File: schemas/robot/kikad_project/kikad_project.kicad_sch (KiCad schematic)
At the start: 50 parts, among them IC1 HCPL-2531, IC2 HCPL-2531, IC3 HCPL-2531, J1 236-102, J10 236-104, J11 236-104, J12 236-744, J13 236-102, J14 236-102, J15 236-102, J16 236-102, J17 236-744, J18 236-102, J2 236-104, J3 236-102, J4 236-102, J5 236-744, J6 236-102, J7 236-102, J8 236-744, J9 236-102, Q2 IRF5305PbF, U1 NRF24L01_Breakout, U12 CD40109BE, U2 STM32F103C8T6, U3 L7805, U4 L7805, X1 3522-2

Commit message: small edits to robot PCB schema and pcb layout
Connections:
- net DISK_DIR: now also IC1.4 (VF2+), U2.14 (PA4); no longer IC1.3 (VIN-), U2.16 (PA6)
- net DISK_PWM: now also IC1.1 (VF1+); no longer IC1.2 (VIN+)
- net GND: now also IC1.2 (VF1-), IC1.3 (VF2-), IC2.2 (VF1-), IC2.3 (VF2-), IC3.2 (VF1-), IC3.3 (VF2-); no longer IC1.4 (GND1), IC2.4 (GND1), IC3.4 (GND1)
- net VCC: no longer IC1.1 (VDD1), IC2.1 (VDD1), IC3.1 (VDD1)
- net WHEEL_LEFT_DIR: now also IC2.4 (VF2+); no longer IC2.3 (VIN-)
- net WHEEL_LEFT_PWM: now also IC2.1 (VF1+); no longer IC2.2 (VIN+)
- net WHEEL_RIGHT_DIR: now also IC3.4 (VF2+), U2.16 (PA6); no longer IC3.3 (VIN-), U2.14 (PA4)
- net WHEEL_RIGHT_PWM: now also IC3.1 (VF1+); no longer IC3.2 (VIN+)

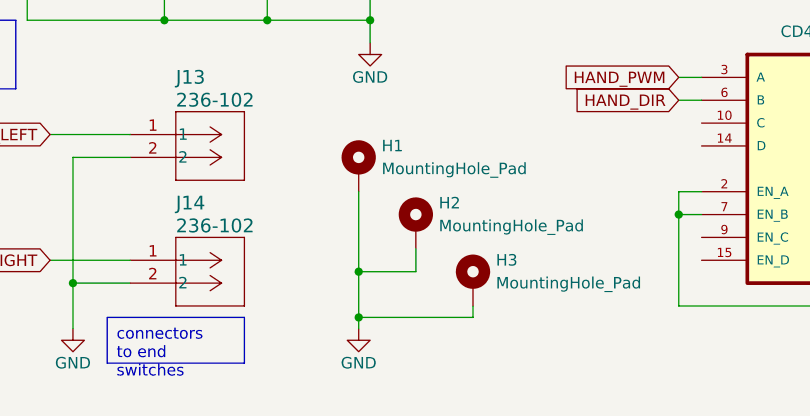
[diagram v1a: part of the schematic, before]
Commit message: small changes to the PCB layout
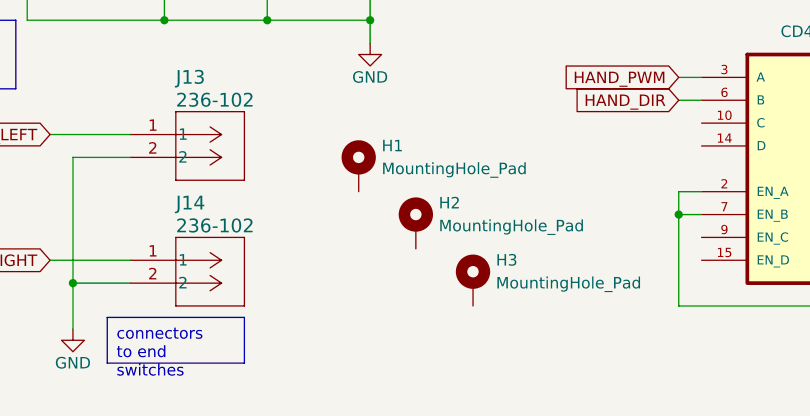
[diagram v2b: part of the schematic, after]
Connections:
- net GND: no longer H1.1, H2.1, H3.1
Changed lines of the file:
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@@
   (junction (at 135.89 161.29) (diameter 0) (color 0 0 0 0)
   )
-  (junction (at 68.58 182.88) (diameter 0) (color 0 0 0 0)
-  )
   (junction (at 238.76 143.51) (diameter 0) (color 0 0 0 0)
   )
@@
   (junction (at 140.97 185.42) (diameter 0) (color 0 0 0 0)
   )
-  (junction (at 68.58 187.96) (diameter 0) (color 0 0 0 0)
-  )
   (junction (at 58.42 142.24) (diameter 0) (color 0 0 0 0)
   )
@@
     (stroke (width 0) (type default))
   )
-  (wire (pts (xy 68.58 182.88) (xy 74.93 182.88))
-    (stroke (width 0) (type default))
-  )
   (wire (pts (xy 109.22 63.5) (xy 111.76 63.5))
     (stroke (width 0) (type default))
@@
     (stroke (width 0) (type default))
   )
-  (wire (pts (xy 68.58 187.96) (xy 68.58 189.23))
-    (stroke (width 0) (type default))
-  )
   (wire (pts (xy 46.99 83.82) (xy 46.99 87.63))
     (stroke (width 0) (type default))
@@
     (stroke (width 0) (type default))
   )
-  (wire (pts (xy 68.58 173.99) (xy 68.58 182.88))
-    (stroke (width 0) (type default))
-  )
   (wire (pts (xy 142.24 63.5) (xy 144.78 63.5))
     (stroke (width 0) (type default))
@@
     (stroke (width 0) (type default))
   )
-  (wire (pts (xy 74.93 180.34) (xy 74.93 182.88))
-    (stroke (width 0) (type default))
-  )
   (wire (pts (xy 140.97 168.91) (xy 140.97 173.99))
     (stroke (width 0) (type default))
@@
     (stroke (width 0) (type default))
   )
-  (wire (pts (xy 68.58 182.88) (xy 68.58 187.96))
-    (stroke (width 0) (type default))
-  )
   (wire (pts (xy 140.97 163.83) (xy 140.97 161.29))
     (stroke (width 0) (type default))
@@
     (stroke (width 0) (type default))
   )
-  (wire (pts (xy 68.58 187.96) (xy 81.28 187.96))
-    (stroke (width 0) (type default))
-  )
   (wire (pts (xy 69.85 86.36) (xy 69.85 87.63))
     (stroke (width 0) (type default))
@@
   )
   (wire (pts (xy 238.76 38.1) (xy 243.84 38.1))
-    (stroke (width 0) (type default))
-  )
-  (wire (pts (xy 81.28 186.69) (xy 81.28 187.96))
     (stroke (width 0) (type default))
   )
@@
         )
       )
-    )
-  )
-  (symbol (lib_id "power:GND") (at 68.58 189.23 0) (unit 1)
-    (in_bom yes) (on_board yes) (dnp no)
-    (property "Reference" "#PWR020" (at 68.58 195.58 0)
-      (effects (font (size 1.27 1.27)) hide)
-    )
-    (property "Value" "GND" (at 68.58 193.04 0)
-      (effects (font (size 1.27 1.27)))
-    )
-    (property "Footprint" "" (at 68.58 189.23 0)
-      (effects (font (size 1.27 1.27)) hide)
-    )
-    (property "Datasheet" "" (at 68.58 189.23 0)
-      (effects (font (size 1.27 1.27)) hide)
-    )
-    (pin "1")
-    (instances
-      (project "kikad_project"
-        (path "/d2a66178-d1ee-482f-bb26-256f544868a0"
-          (reference "#PWR020") (unit 1)
-        )
-      )

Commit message: regular upload
1. mid production documentation
2. minor edits on the electrical schemas
3. small changes to the 3d model of the robot
4. first try to wrtie the necessary code
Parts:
- C10: value 100uF -> 10nF
- C11, C12: value 100uF -> 10F
- J12, J17, J5, J8: value 236-744 -> 236-401
- Q2: value IRF5305PbF -> IXTP120P065T
- R2, R3, R4: value 6.8МR -> 68R
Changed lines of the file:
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@@
+    (effects (font (size 1.27 1.27)) (justify left top))
+  )
+  (text_box "diod da pazi da ne se razredqt kondenzatorite"
+    (at 19.05 78.74 0) (size 3.81 3.81)
+    (stroke (width 0) (type default))
+    (fill (type none))
     (effects (font (size 1.27 1.27)) (justify left top))
   )
@@
   (symbol (lib_id "Device:C") (at 123.19 138.43 0) (mirror y) (unit 1)
     (in_bom yes) (on_board yes) (dnp no)
-    (property "Reference" "C12" (at 127 135.89 0)
-      (effects (font (size 1.27 1.27)) (justify left))
-    )
-    (property "Value" "100uF" (at 130.81 140.97 0)
+    (property "Reference" "C12" (at 128.27 135.89 0)
+      (effects (font (size 1.27 1.27)) (justify left))
+    )
+    (property "Value" "10F" (at 128.27 140.97 0)
       (effects (font (size 1.27 1.27)) (justify left))
     )
@@
       (effects (font (size 1.27 1.27)) (justify left))
     )
-    (property "Value" "6.8МR" (at 134.62 134.62 90)
+    (property "Value" "68R" (at 134.62 134.62 90)
       (effects (font (size 1.27 1.27)) (justify left))
     )
@@
       (effects (font (size 1.27 1.27)))
     )
-    (property "Value" "IRF5305PbF" (at 58.42 128.27 90)
+    (property "Value" "IXTP120P065T" (at 58.42 128.27 90)
       (effects (font (size 1.27 1.27)))
     )
@@
   (symbol (lib_id "Device:C") (at 123.19 102.87 0) (mirror y) (unit 1)
     (in_bom yes) (on_board yes) (dnp no)
-    (property "Reference" "C10" (at 127 100.33 0)
-      (effects (font (size 1.27 1.27)) (justify left))
-    )
-    (property "Value" "100uF" (at 130.81 105.41 0)
+    (property "Reference" "C10" (at 128.27 100.33 0)
+      (effects (font (size 1.27 1.27)) (justify left))
+    )
+    (property "Value" "10nF" (at 129.54 105.41 0)
       (effects (font (size 1.27 1.27)) (justify left))
     )
@@
       (effects (font (size 1.27 1.27)) (justify left))
     )
-    (property "Value" "6.8МR" (at 134.62 116.84 90)
+    (property "Value" "68R" (at 134.62 116.84 90)
       (effects (font (size 1.27 1.27)) (justify left))
     )
@@
       (effects (font (size 1.524 1.524)) (justify left))
     )
-    (property "Value" "236-744" (at 248.92 85.09 0)
+    (property "Value" "236-401" (at 248.92 85.09 0)
       (effects (font (size 1.524 1.524)) (justify left))
     )
@@
   (symbol (lib_id "Device:C") (at 123.19 120.65 0) (mirror y) (unit 1)
     (in_bom yes) (on_board yes) (dnp no)
-    (property "Reference" "C11" (at 127 118.11 0)
-      (effects (font (size 1.27 1.27)) (justify left))
-    )
-    (property "Value" "100uF" (at 130.81 123.19 0)
+    (property "Reference" "C11" (at 128.27 118.11 0)
+      (effects (font (size 1.27 1.27)) (justify left))
+    )
+    (property "Value" "10F" (at 128.27 123.19 0)
       (effects (font (size 1.27 1.27)) (justify left))
     )
@@
       (effects (font (size 1.524 1.524)) (justify left))
     )
-    (property "Value" "236-744" (at 152.4 130.81 0)
+    (property "Value" "236-401" (at 152.4 130.81 0)
       (effects (font (size 1.524 1.524)) (justify left))
     )
@@
       (effects (font (size 1.27 1.27)) (justify left))
     )
-    (property "Value" "6.8МR" (at 134.62 99.06 90)
+    (property "Value" "68R" (at 134.62 99.06 90)
       (effects (font (size 1.27 1.27)) (justify left))
     )
@@
       (effects (font (size 1.524 1.524)) (justify left))
     )
-    (property "Value" "236-744" (at 248.92 135.89 0)
+    (property "Value" "236-401" (at 248.92 135.89 0)
       (effects (font (size 1.524 1.524)) (justify left))
     )
@@
       (effects (font (size 1.524 1.524)) (justify left))
     )
-    (property "Value" "236-744" (at 248.92 34.29 0)
-      (effects (font (size 1.524 1.524)) (justify left))
-    )
+    (property "Value" "236-401" (at 248.92 34.29 0)
+      (effects (font (size 1.524 1.524)) (justify left))
+    )

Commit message: PCB edit + other minor changes
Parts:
- removed U2: STM32F103C8T6, Library:STM32F103C8T6_pinout, symbol STM32F103C8T6:STM32F103C8T6_pinout
- added U2: STM32F103C8T6, Library:STM32F103C8T6_pinout, symbol Robot_Symbols:STM32F103C8T6_pinout
- C10: value 10nF -> 100nF
- C11, C12: value 10F -> 100nF
- R2, R3, R4: value 68R -> 680R
- renumbered Q2 to Q1
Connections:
- net +3.3V: now also U2.5 (3V3), U2.6 (3V3)
- net DISK_DIR: now also U2.14 (PA4)
- net DISK_PWM: now also U2.17 (PA7)
- net GND: now also U2.20 (GND), U2.23 (GND), U2.9 (GND)
- net HAND_DIR: now also U2.12 (PA2)
- net HAND_END_LEFT: now also U2.28 (PB15)
- net HAND_END_RIGHT: now also U2.27 (PB14)
- net HAND_PWM: now also U2.11 (PA1)
- net OPT_END_DISK: now also U2.46 (PB9)
- net OPT_END_WHEEL_LEFT: now also U2.45 (PB8)
- net OPT_END_WHEEL_RIGHT: now also U2.43 (PB7)
- net PB3: now also U2.39 (PB3)
- net PB4: now also U2.40 (PB4)
- net PB5: now also U2.41 (PB5)
- net VCC: now also U2.8 (5V)
- net WHEEL_LEFT_DIR: now also U2.15 (PA5)
- net WHEEL_LEFT_PWM: now also U2.18 (PB0)
- net WHEEL_RIGHT_DIR: now also U2.16 (PA6)
- net WHEEL_RIGHT_PWM: now also U2.19 (PB1)
- net PA10 renamed NRF24L01_CE
- net NRF24L01_CE: now also U2.32 (PA11)
- net PA15 renamed NRF24L01_CSN
- net NRF24L01_CSN: now also U2.38 (PA15)
- net PA9 renamed NRF24L01_IRQ
- net NRF24L01_IRQ: now also U2.31 (PA10)
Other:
- moved on the sheet: C1, C2, C3, C4, C5, C6, C7, C8, C9, D1, D3, J1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

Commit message: robot schema edit
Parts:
- added RN1: R_Network06, Resistor_THT:R_Array_SIP7, symbol Device:R_Network06
- added RN2: R_Pack06_SIP, Resistor_THT:R_Array_SIP12, symbol Device:R_Pack06_SIP
- C10, C11, C12: footprint Capacitor_THT:CP_Radial_D5.0mm_P2.00mm -> Capacitor_THT:C_Rect_L4.6mm_W3.8mm_P2.50mm_MKS02_FKP02
- C2, C3, C4, C6, C7, C9: footprint Capacitor_THT:C_Axial_L5.1mm_D3.1mm_P7.50mm_Horizontal -> Capacitor_THT:C_Rect_L4.6mm_W3.8mm_P2.50mm_MKS02_FKP02
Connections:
- net +24V: now also Q1.3 (D); no longer Q1.2 (D)
- net +5V: now also RN1.1 (common)
- net DISK_DIR: now also RN2.3 (R2.1); no longer IC1.4 (VF2+)
- net DISK_PWM: now also RN2.1 (R1.1); no longer IC1.1 (VF1+)
- net WHEEL_LEFT_DIR: now also RN2.7 (R4.1); no longer IC2.4 (VF2+)
- net WHEEL_LEFT_PWM: now also RN2.5 (R3.1); no longer IC2.1 (VF1+)
- net WHEEL_RIGHT_DIR: now also RN2.11 (R6.1); no longer IC3.4 (VF2+)
- net WHEEL_RIGHT_PWM: now also RN2.9 (R5.1); no longer IC3.1 (VF1+)
- net IC1_VO2: now reaches IC1.6 (V02), J4.1
- net IC1_VO2: now also RN1.3 (R2)
- net IC1_VO1: now reaches IC1.7 (V01), J4.2
- net IC1_VO1: now also RN1.2 (R1)
- net at D3.A, X1.2A, X1.2B: now also Q1.2 (S); no longer Q1.3 (S)
- net IC2_VO2: now reaches IC2.6 (V02), J7.1
- net IC2_VO2: now also RN1.5 (R4)
- net IC2_VO1: now reaches IC2.7 (V01), J7.2
- net IC2_VO1: now also RN1.4 (R3)
- net IC3_VO2: now reaches IC3.6 (V02), J16.1
- net IC3_VO2: now also RN1.7 (R6)
- net IC3_VO1: now reaches IC3.7 (V01), J16.2
- net IC3_VO1: now also RN1.6 (R5)
- new net IC1_VF1+: IC1.1 (VF1+), RN2.2 (R1.2)
- new net IC1_VF2+: IC1.4 (VF2+), RN2.4 (R2.2)
- new net IC2_VF1+: IC2.1 (VF1+), RN2.6 (R3.2)
- new net IC2_VF2+: IC2.4 (VF2+), RN2.8 (R4.2)
- new net IC3_VF1+: IC3.1 (VF1+), RN2.10 (R5.2)
- new net IC3_VF2+: IC3.4 (VF2+), RN2.12 (R6.2)
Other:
- moved on the sheet: IC1, J4, J5, J6
